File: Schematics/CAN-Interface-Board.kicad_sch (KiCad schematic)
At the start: 0 parts

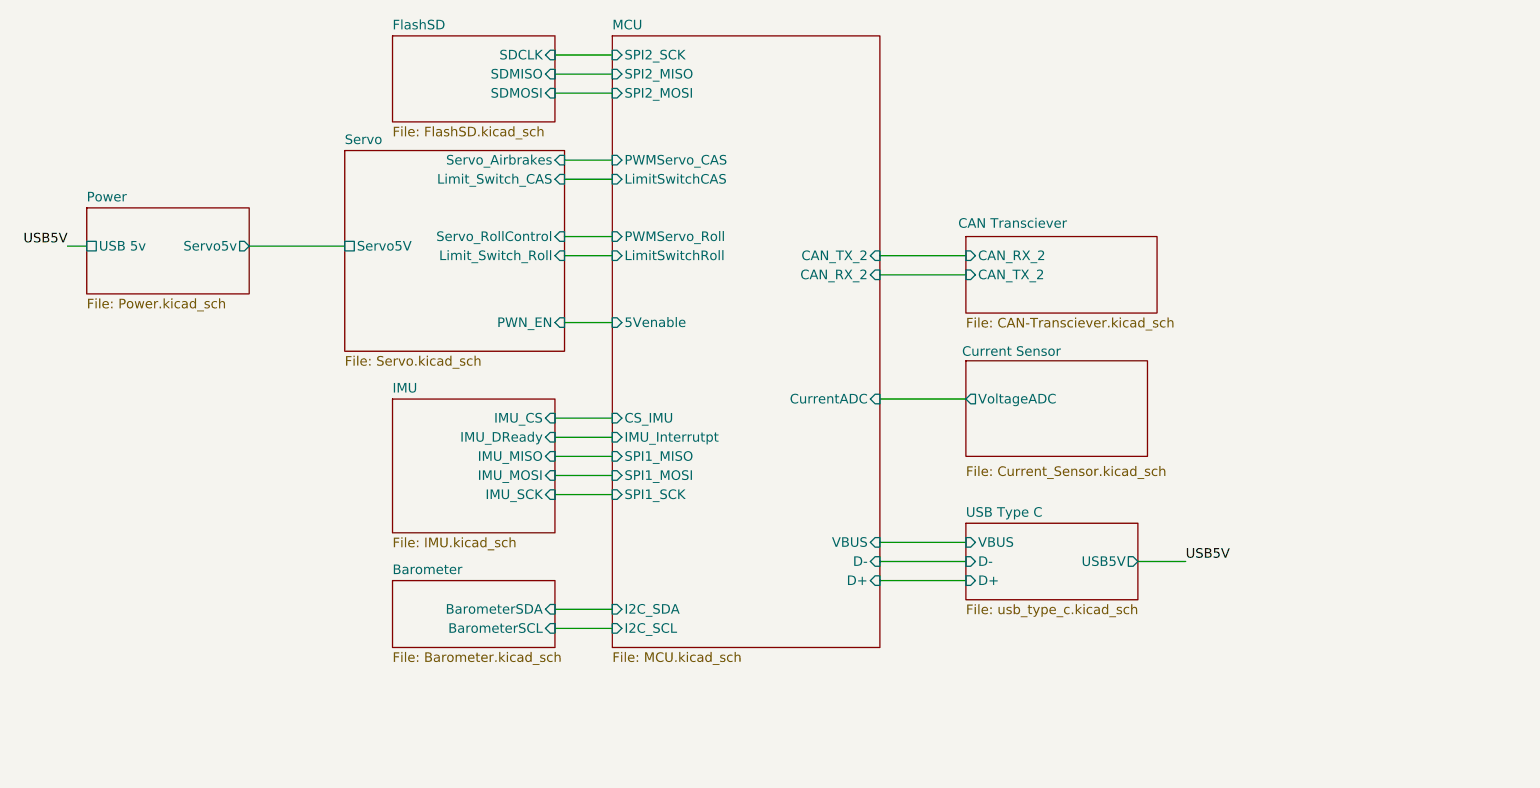
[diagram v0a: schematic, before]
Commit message: started new design with esp32
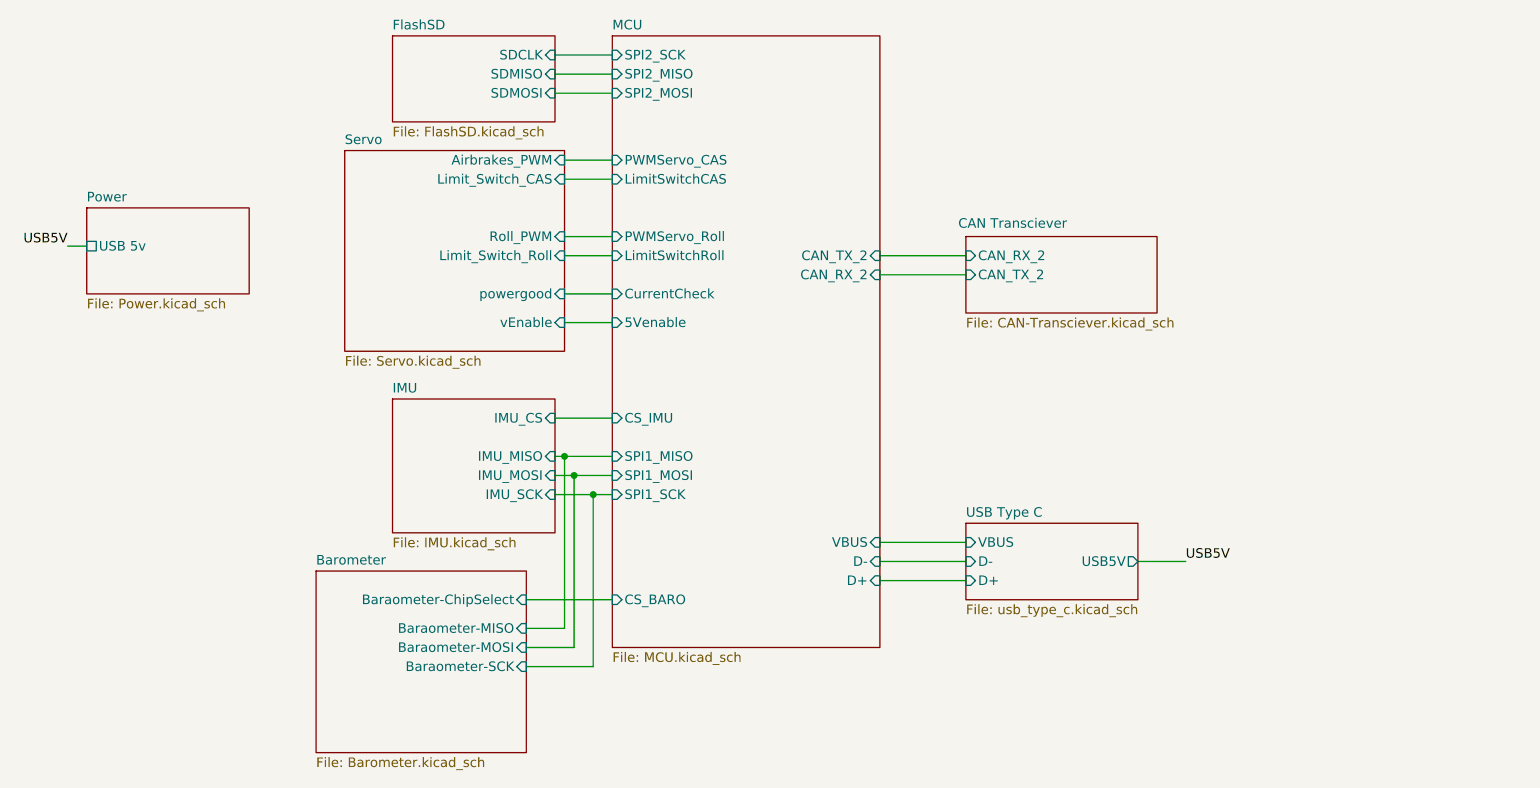
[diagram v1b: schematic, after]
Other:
- removed sheet Current Sensor
- sheet Barometer ports: added Baraometer-ChipSelect, Baraometer-MISO, Baraometer-MOSI, Baraometer-SCK; removed BarometerSCL, BarometerSDA
- sheet IMU ports: added none; removed IMU_DReady
- sheet MCU ports: added CS_BARO, CurrentCheck; removed CurrentADC, I2C_SCL, I2C_SDA, IMU_Interrutpt
- sheet Power ports: added none; removed Servo5v
- sheet Servo ports: added Airbrakes_PWM, Roll_PWM, powergood, vEnable; removed PWN_EN, Servo5V, Servo_Airbrakes, Servo_RollControl

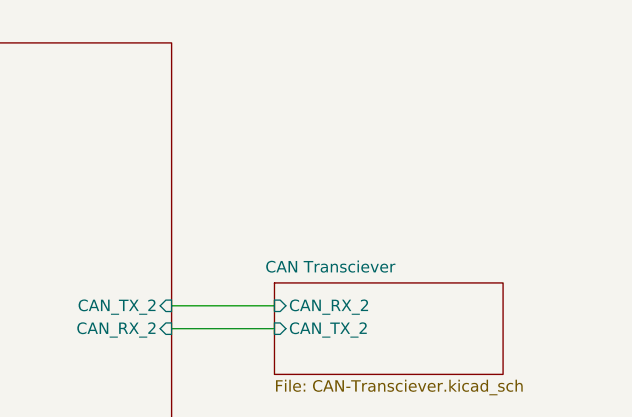
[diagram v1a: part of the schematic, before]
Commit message: added esp32 for uart to tune control systems from a web browser app
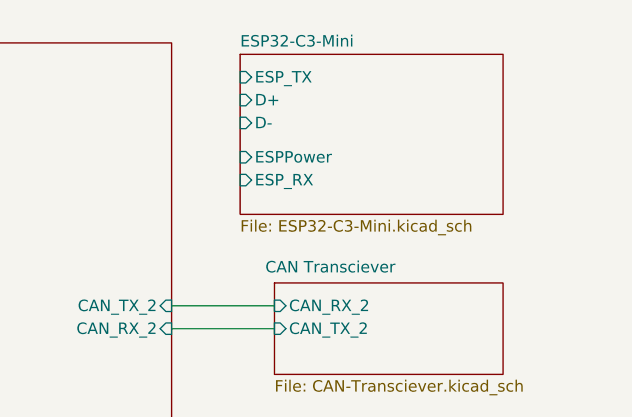
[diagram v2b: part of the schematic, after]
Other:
- added sheet ESP32-C3-Mini (ESP32-C3-Mini.kicad_sch)
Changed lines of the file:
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@@
+	)
+	(sheet
+		(at 177.8 60.96)
+		(size 29.21 17.78)
+		(exclude_from_sim no)
+		(in_bom yes)
+		(on_board yes)
+		(dnp no)
+		(fields_autoplaced yes)
+		(stroke
+			(width 0.1524)
+			(type solid)
+		)
+		(fill
+			(color 0 0 0 0.0000)
+		)
+		(property "Sheetname" "ESP32-C3-Mini"
+			(at 177.8 60.2484 0)
+			(effects
+				(font
+					(size 1.27 1.27)
+				)
+				(justify left bottom)
+			)
+		)
+		(property "Sheetfile" "ESP32-C3-Mini.kicad_sch"
+			(at 177.8 79.3246 0)
+			(effects
+				(font
+					(size 1.27 1.27)
+				)
+				(justify left top)
+			)
+		)
+		(pin "D+" input
+			(at 177.8 66.04 180)
+			(effects
+				(font
+					(size 1.27 1.27)
+				)
+				(justify left)
+			)
+		)
+		(pin "D-" input
+			(at 177.8 68.58 180)
+			(effects
+				(font
+					(size 1.27 1.27)
+				)
+				(justify left)
+			)
+		)
+		(pin "ESPPower" input
+			(at 177.8 72.39 180)
+			(effects
+				(font
+					(size 1.27 1.27)
+				)
+				(justify left)
+			)
+		)
+		(pin "ESP_RX" input
+			(at 177.8 74.93 180)
+			(effects
+				(font
+					(size 1.27 1.27)
+				)
+				(justify left)
+			)
+		)
+		(pin "ESP_TX" input
+			(at 177.8 63.5 180)
+			(effects
+				(font
+					(size 1.27 1.27)
+				)
+				(justify left)
+			)
+		)
+		(instances
+			(project "CAN-Interface-Board"
+				(path "/8a3e7f99-4046-40e8-bd7c-d9d1c8c7162e"
+					(page "10")
+				)
+			)
+		)
 	)
 	(sheet

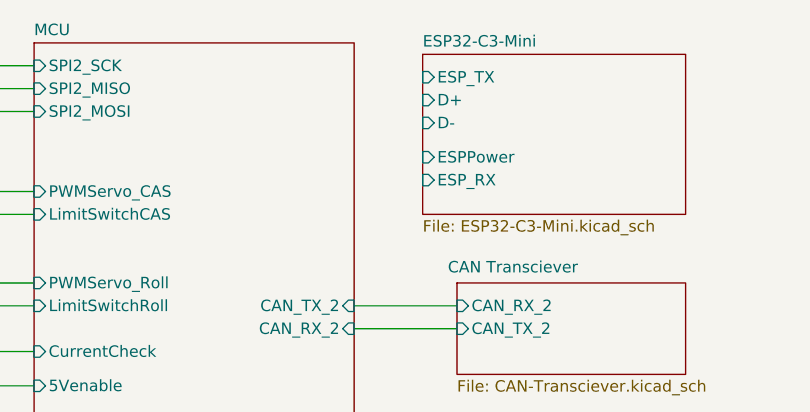
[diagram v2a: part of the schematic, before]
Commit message: clean up of routing
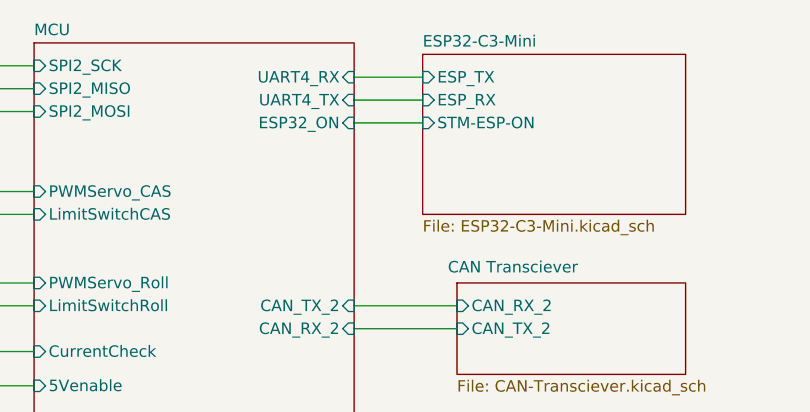
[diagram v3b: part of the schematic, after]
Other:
- sheet ESP32-C3-Mini ports: added STM-ESP-ON; removed D+, D-, ESPPower
- sheet MCU ports: added ESP32_ON, UART4_RX, UART4_TX; removed none
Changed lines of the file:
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@@
+	(wire
+		(pts
+			(xy 170.18 68.58) (xy 177.8 68.58)
+		)
+		(stroke
+			(width 0)
+			(type default)
+		)
+	)
 	(wire
 		(pts
@@
 	(wire
 		(pts
+			(xy 170.18 63.5) (xy 177.8 63.5)
+		)
+		(stroke
+			(width 0)
+			(type default)
+		)
+	)
+	(wire
+		(pts
 			(xy 128.27 115.57) (xy 128.27 138.43)
 		)
@@
 		(pts
 			(xy 127 110.49) (xy 134.62 110.49)
+		)
+		(stroke
+			(width 0)
+			(type default)
+		)
+	)
+	(wire
+		(pts
+			(xy 170.18 66.04) (xy 177.8 66.04)
 		)
 		(stroke
@@
 			)
 		)
-		(pin "D+" input
+		(pin "ESP_RX" input
 			(at 177.8 66.04 180)
-			(effects
-				(font
-					(size 1.27 1.27)
-				)
-				(justify left)
-			)
-		)
-		(pin "D-" input
-			(at 177.8 68.58 180)
-			(effects
-				(font
-					(size 1.27 1.27)
-				)
-				(justify left)
-			)
-		)
-		(pin "ESPPower" input
-			(at 177.8 72.39 180)
-			(effects
-				(font
-					(size 1.27 1.27)
-				)
-				(justify left)
-			)
-		)
-		(pin "ESP_RX" input
-			(at 177.8 74.93 180)
 			(effects
 				(font
@@
 		(pin "ESP_TX" input
 			(at 177.8 63.5 180)
+			(effects
+				(font
+					(size 1.27 1.27)
+				)
+				(justify left)
+			)
+		)
+		(pin "STM-ESP-ON" input
+			(at 177.8 68.58 180)
 			(effects
 				(font
@@
 			)
 		)
+		(pin "UART4_RX" input
+			(at 170.18 63.5 0)
+			(effects
+				(font
+					(size 1.27 1.27)
+				)
+				(justify right)
+			)
+		)
+		(pin "UART4_TX" input
+			(at 170.18 66.04 0)
+			(effects
+				(font
+					(size 1.27 1.27)
+				)
+				(justify right)
+			)
+		)
+		(pin "ESP32_ON" input
+			(at 170.18 68.58 0)
+			(effects
+				(font
+					(size 1.27 1.27)
+				)
+				(justify right)
+			)
+		)

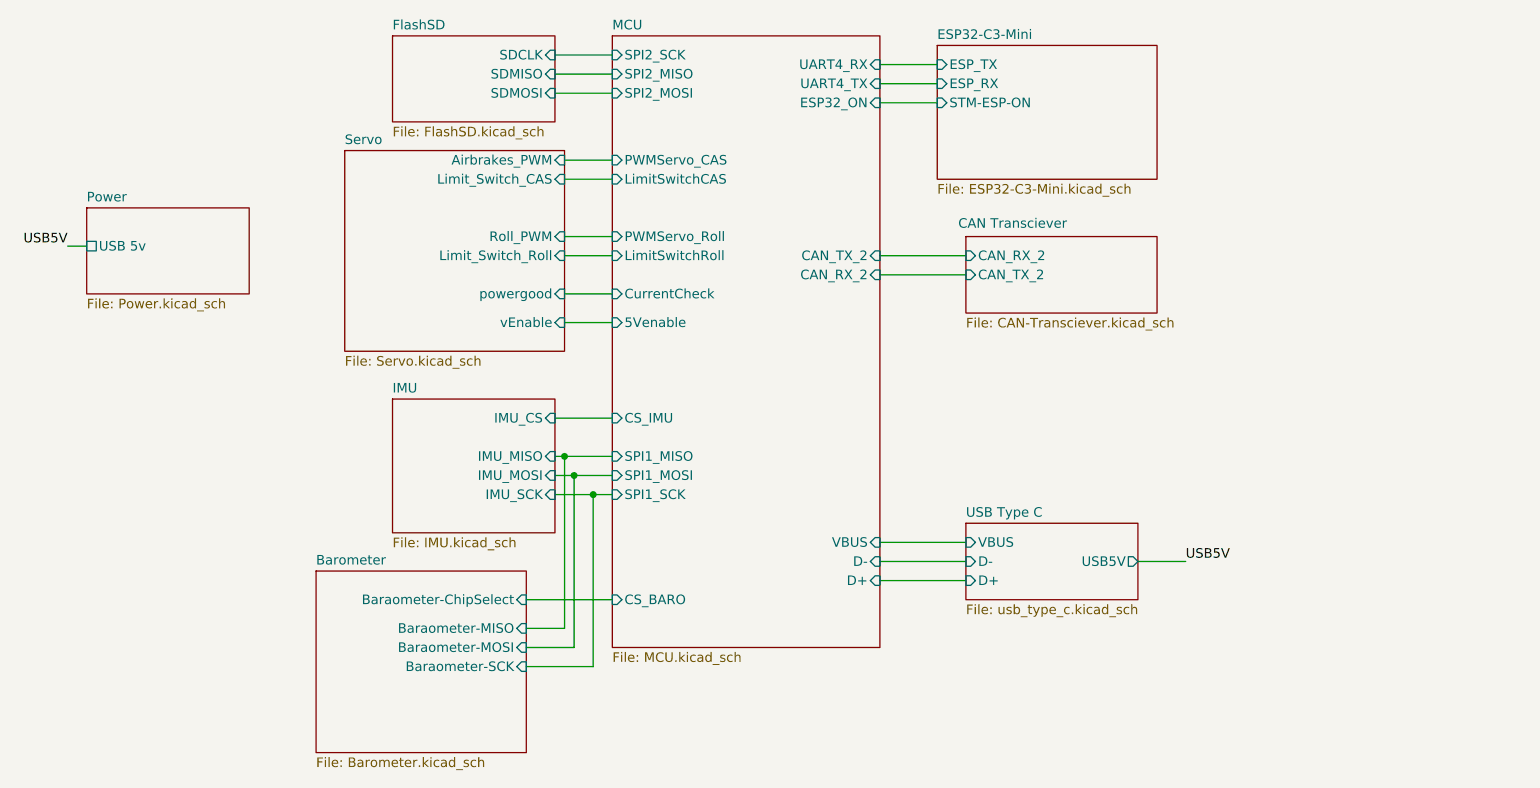
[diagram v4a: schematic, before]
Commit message: removed esp32 to seperate board, added gps breakout, pending final review for purchase
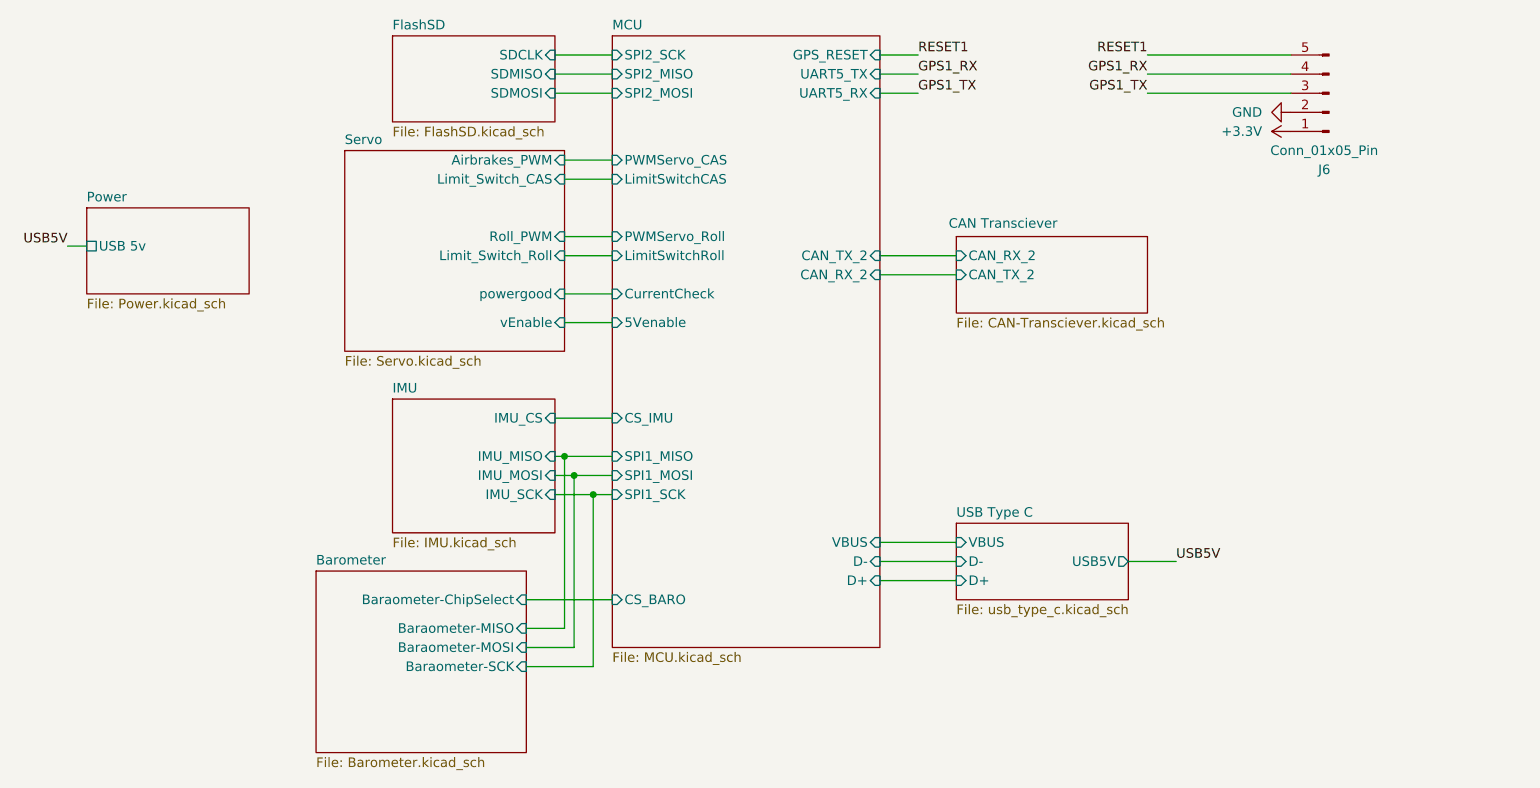
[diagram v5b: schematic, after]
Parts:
- added J6: Conn_01x05_Pin, Connector_JST:JST_XH_B5B-XH-A_1x05_P2.50mm_Vertical, symbol Connector:Conn_01x05_Pin
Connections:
- new net +3.3V: J6.1 (Pin_1)
- new net GND: J6.2 (Pin_2)
- new net GPS1_RX: J6.4 (Pin_4)
- new net GPS1_TX: J6.3 (Pin_3)
- new net RESET1: J6.5 (Pin_5)
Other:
- removed sheet ESP32-C3-Mini
- sheet MCU ports: added GPS_RESET, UART5_RX, UART5_TX; removed ESP32_ON, UART4_RX, UART4_TX

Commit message: finished waiting for review
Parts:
- added C1: 100nf, Capacitor_SMD:C_0805_2012Metric_Pad1.18x1.45mm_HandSolder, symbol Device:C
- added R1, R11: 27r, Resistor_SMD:R_0805_2012Metric_Pad1.20x1.40mm_HandSolder, symbol Device:R
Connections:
- net GND: now also C1.2
- net MCU/D+: now also R1.1
- net MCU/D-: now also R11.1
- net MCU/VBUS: now also C1.1
- new net USB Type C/D+: R1.2
- new net USB Type C/D-: R11.2

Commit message: final draft, in JLPCB cart
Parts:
- C1: LCSC (none) -> C49678
- J6: now in the parts list
- R1, R11: LCSC (none) -> C17594
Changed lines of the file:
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@@
 		(body_style 1)
 		(exclude_from_sim no)
-		(in_bom no)
+		(in_bom yes)
 		(on_board yes)
 		(in_pos_files yes)
@@
 			)
 		)
-		(property "Description" "Generic connector, single row, 01x05, script generated"
+		(property "Description" ""
 			(at 229.87 67.31 0)
 			(hide yes)
@@
 		)
 		(property "STANDARD" ""
+			(at 229.87 67.31 0)
+			(hide yes)
+			(show_name no)
+			(do_not_autoplace no)
+			(effects
+				(font
+					(size 1.27 1.27)
+				)
+			)
+		)
+		(property "SnapEDA_Link" ""
+			(at 229.87 67.31 0)
+			(hide yes)
+			(show_name no)
+			(do_not_autoplace no)
+			(effects
+				(font
+					(size 1.27 1.27)
+				)
+			)
+		)
+		(property "DESCRIPTION" ""
 			(at 229.87 67.31 0)
 			(hide yes)
@@
 			)
 		)
-		(property "Description" "Unpolarized capacitor"
+		(property "Description" ""
+			(at 176.53 130.81 0)
+			(hide yes)
+			(show_name no)
+			(do_not_autoplace no)
+			(effects
+				(font
+					(size 1.27 1.27)
+				)
+			)
+		)
+		(property "SnapEDA_Link" ""
+			(at 176.53 130.81 0)
+			(hide yes)
+			(show_name no)
+			(do_not_autoplace no)
+			(effects
+				(font
+					(size 1.27 1.27)
+				)
+			)
+		)
+		(property "LCSC" "C49678"
+			(at 176.53 130.81 0)
+			(hide yes)
+			(show_name no)
+			(do_not_autoplace no)
+			(effects
+				(font
+					(size 1.27 1.27)
+				)
+			)
+		)
+		(property "DESCRIPTION" ""
 			(at 176.53 130.81 0)
 			(hide yes)
@@
 			)
 		)
-		(property "Description" "Resistor"
-			(at 191.77 132.08 0)
+		(property "Description" ""
+			(at 191.77 132.08 90)
+			(hide yes)
+			(show_name no)
+			(do_not_autoplace no)
+			(effects
+				(font
+					(size 1.27 1.27)
+				)
+			)
+		)
+		(property "SnapEDA_Link" ""
+			(at 191.77 132.08 90)
+			(hide yes)
+			(show_name no)
+			(do_not_autoplace no)
+			(effects
+				(font
+					(size 1.27 1.27)
+				)
+			)
+		)
+		(property "LCSC" "C17594"
+			(at 191.77 132.08 90)
+			(hide yes)
+			(show_name no)
+			(do_not_autoplace no)
+			(effects
+				(font
+					(size 1.27 1.27)
+				)
+			)
+		)
+		(property "DESCRIPTION" ""
+			(at 191.77 132.08 90)
 			(hide yes)
 			(show_name no)
@@
 			)
 		)
-		(property "Description" "Resistor"
-			(at 203.2 129.54 0)
-			(hide yes)
-			(show_name no)
+		(property "Description" ""
+			(at 203.2 129.54 90)
+			(hide yes)
+			(show_name no)
+			(do_not_autoplace no)
+			(effects
+				(font
+					(size 1.27 1.27)
+				)
+			)
+		)
+		(property "SnapEDA_Link" ""
+			(at 203.2 129.54 90)
+			(hide yes)
+			(show_name no)
+			(do_not_autoplace no)
+			(effects
+				(font
+					(size 1.27 1.27)
+				)
+			)
+		)
+		(property "LCSC" "C17594"
+			(at 203.2 129.54 90)
+			(hide yes)
+			(show_name no)
+			(do_not_autoplace no)
+			(effects
+				(font
+					(size 1.27 1.27)
+				)
+			)
+		)
+		(property "DESCRIPTION" ""
+			(at 203.2 129.54 90)
+			(hide yes)
+			(show_name no)
